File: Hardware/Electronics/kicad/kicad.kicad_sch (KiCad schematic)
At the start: 47 parts, among them J1 Conn_01x03_Socket, J2 Conn_01x03_Socket, J3 Conn_01x03_Socket, J6 USB_C_Receptacle_USB2.0_16P, SW1 SW_Push, SW2 SW_Push, SW3 SW_Push, U1 USBLC6-2P6, U2 MCP73831-2-OT, U3 ESP32-C3-MINI-1-N4, U4 XC6210B332MR, U5 TPS61023DRLR, U6 SN74LV1T34DBV

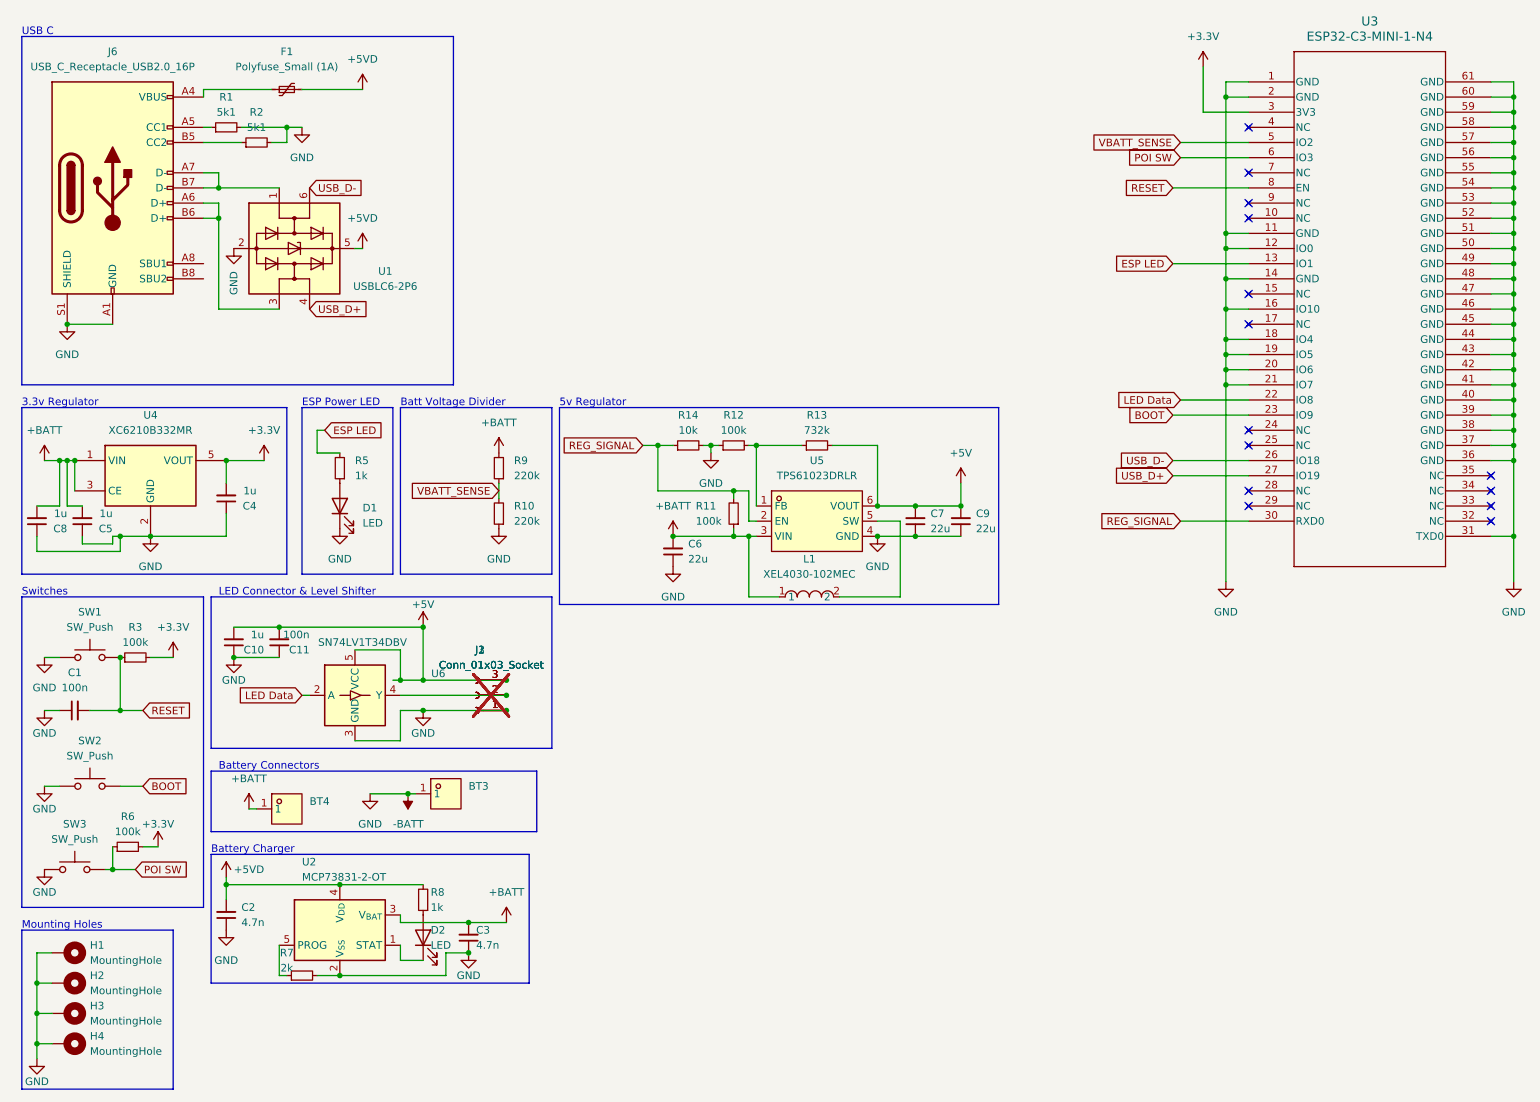
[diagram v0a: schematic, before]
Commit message: Add Clock pinout & FPC connectors to PCB, start on basic ws2812b LED strip.
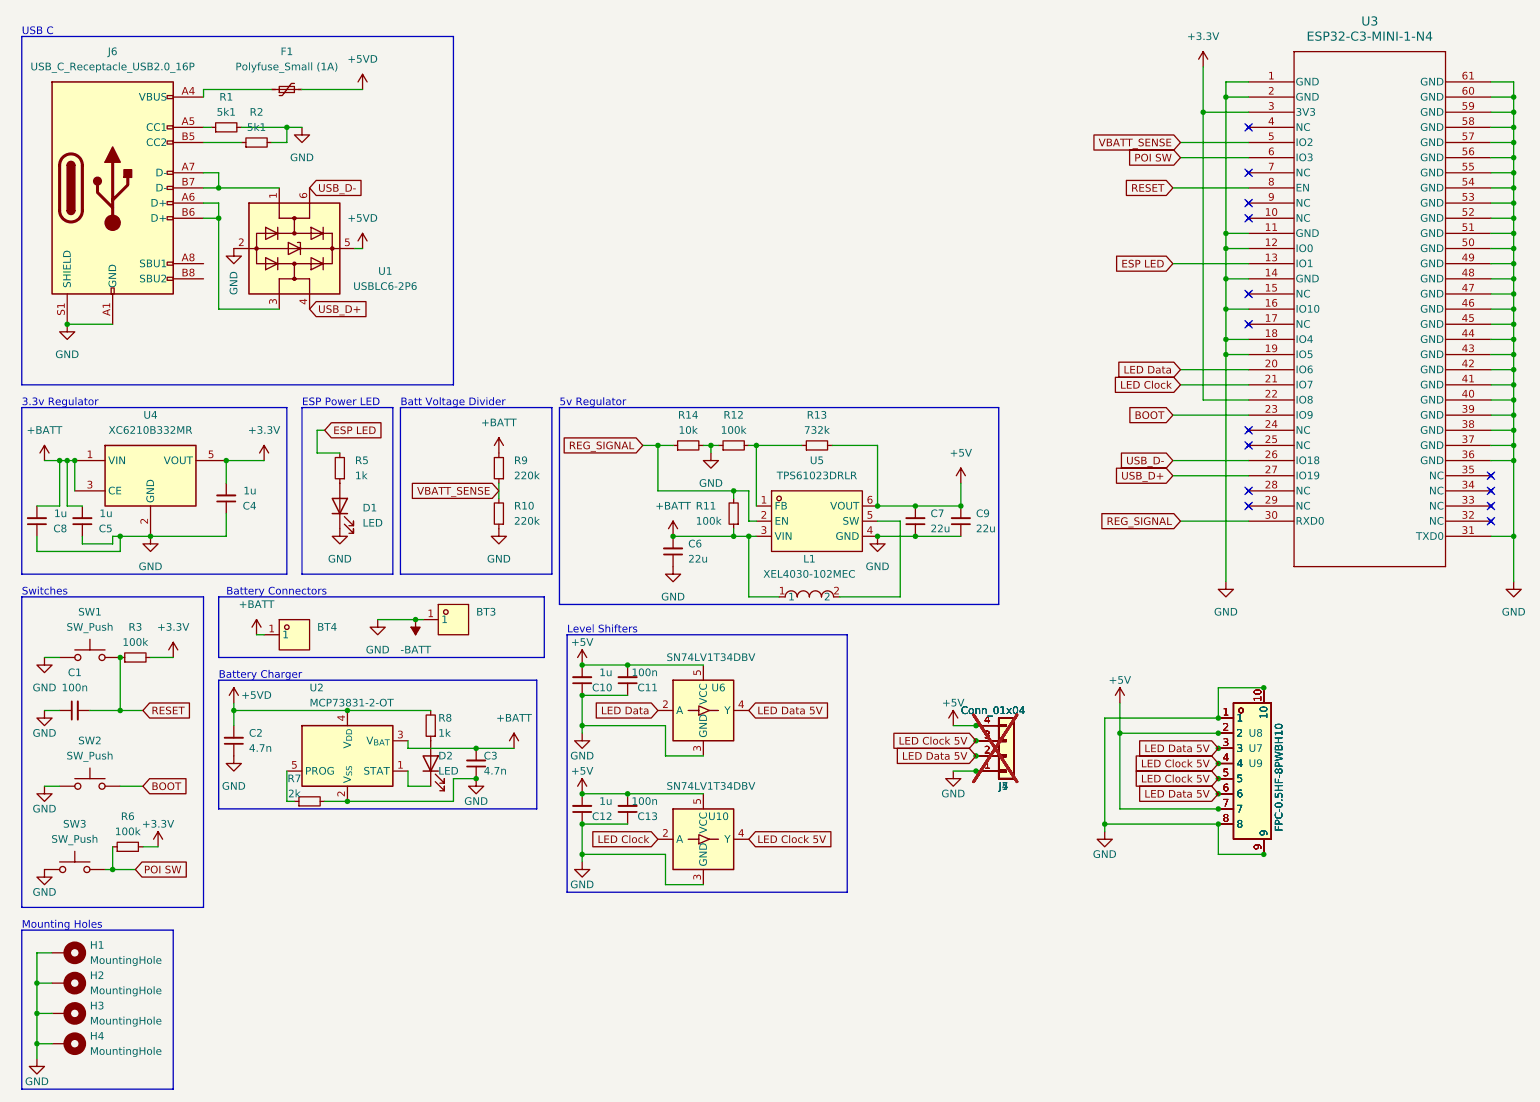
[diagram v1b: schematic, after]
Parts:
- removed J1, J2, J3: Conn_01x03_Socket, Connector_JST:JST_PH_B3B-PH-K_1x03_P2.00mm_Vertical, symbol Connector:Conn_01x03_Socket
- added C12: 1u, Capacitor_SMD:C_0805_2012Metric, symbol Device:C_Small
- added C13: 100n, Capacitor_SMD:C_0805_2012Metric, symbol Device:C_Small
- added J4, J5, J7: Conn_01x04, Connector_PinHeader_2.00mm:PinHeader_1x04_P2.00mm_Vertical, symbol Connector_Generic:Conn_01x04
- added U10: SN74LV1T34DBV, Package_TO_SOT_SMD:SOT-23-5, symbol Logic_LevelTranslator:SN74LV1T34DBV
- added U7, U8, U9: FPC-0.5HF-8PWBH10, easyeda2kicad:FPC-SMD_8P-P0.50_XUNPU_FPC-0.5HF-8PWBH10, symbol easyeda2kicad:FPC-0.5HF-8PWBH10
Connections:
- net +3.3V: now also U3.22 (IO8)
- net +5V: now also C12.2, C13.2, J4.4 (Pin_4), J5.4 (Pin_4), J7.4 (Pin_4), U10.5 (VCC), U7.2, U7.7, U8.2, U8.7, U9.2, U9.7
- net -BATT: now also C12.1, C13.1, J4.1 (Pin_1), J5.1 (Pin_1), J7.1 (Pin_1), U10.3 (GND), U7.1, U7.10, U7.8, U7.9, U8.1, U8.10, U8.8, U8.9, U9.1, U9.10, U9.8, U9.9; no longer U3.20 (IO6), U3.21 (IO7)
- net LED Data: now also U3.20 (IO6); no longer U3.22 (IO8)
- net LED Data 5V: now reaches U6.4 (Y)
- net LED Data 5V: now also J4.2 (Pin_2), J5.2 (Pin_2), J7.2 (Pin_2), U7.3, U7.6, U8.3, U8.6, U9.3, U9.6
- new net LED Clock: U10.2 (A), U3.21 (IO7)
- new net LED Clock 5V: J4.3 (Pin_3), J5.3 (Pin_3), J7.3 (Pin_3), U10.4 (Y), U7.4, U7.5, U8.4, U8.5, U9.4, U9.5
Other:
- note added: "Level Shifters"
- note removed: "LED Connector & Level Shifter"
- moved on the sheet: BT3, BT4, C10, C11, C2, C3, D2, R7, R8, U2, U6

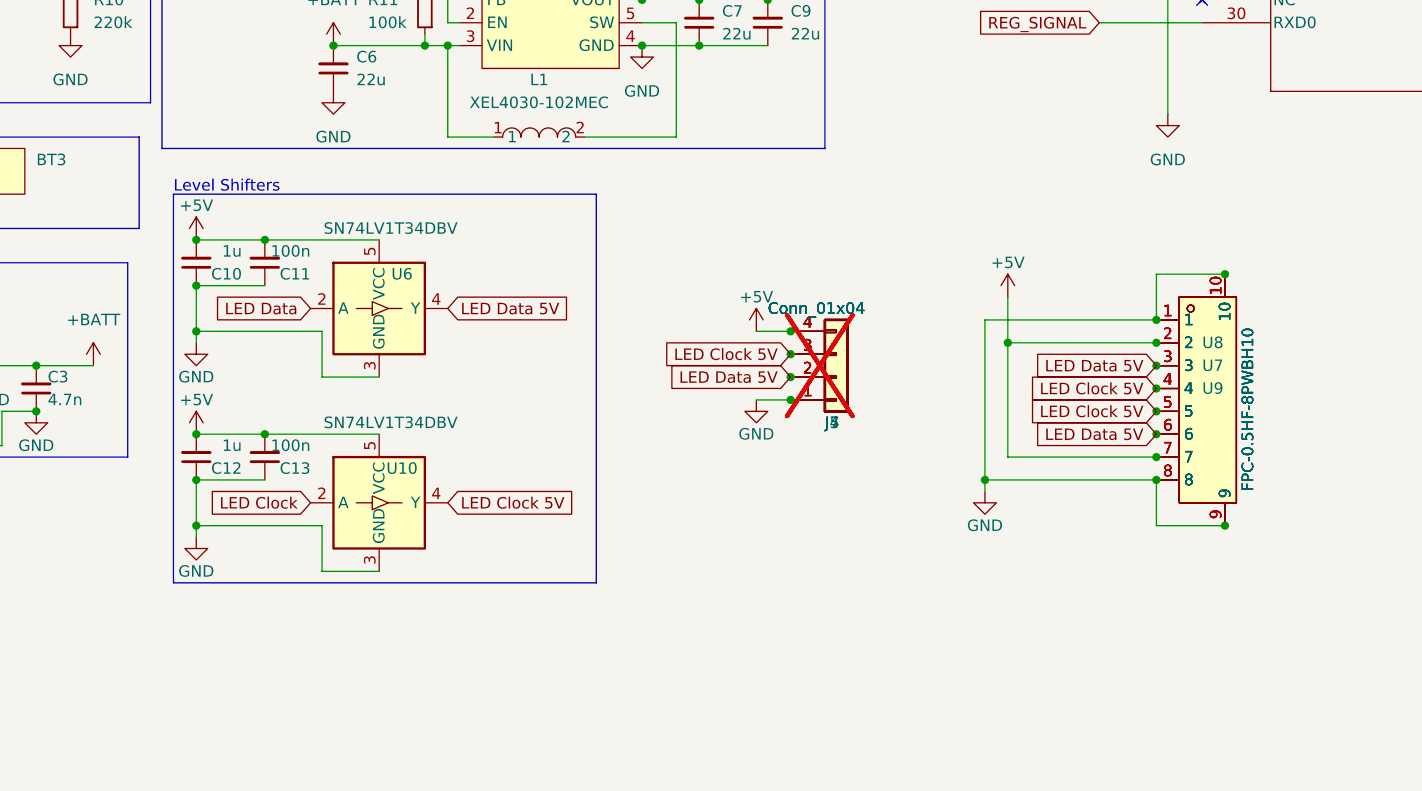
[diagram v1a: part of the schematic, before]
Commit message: Add 20 and 55 pixel strips
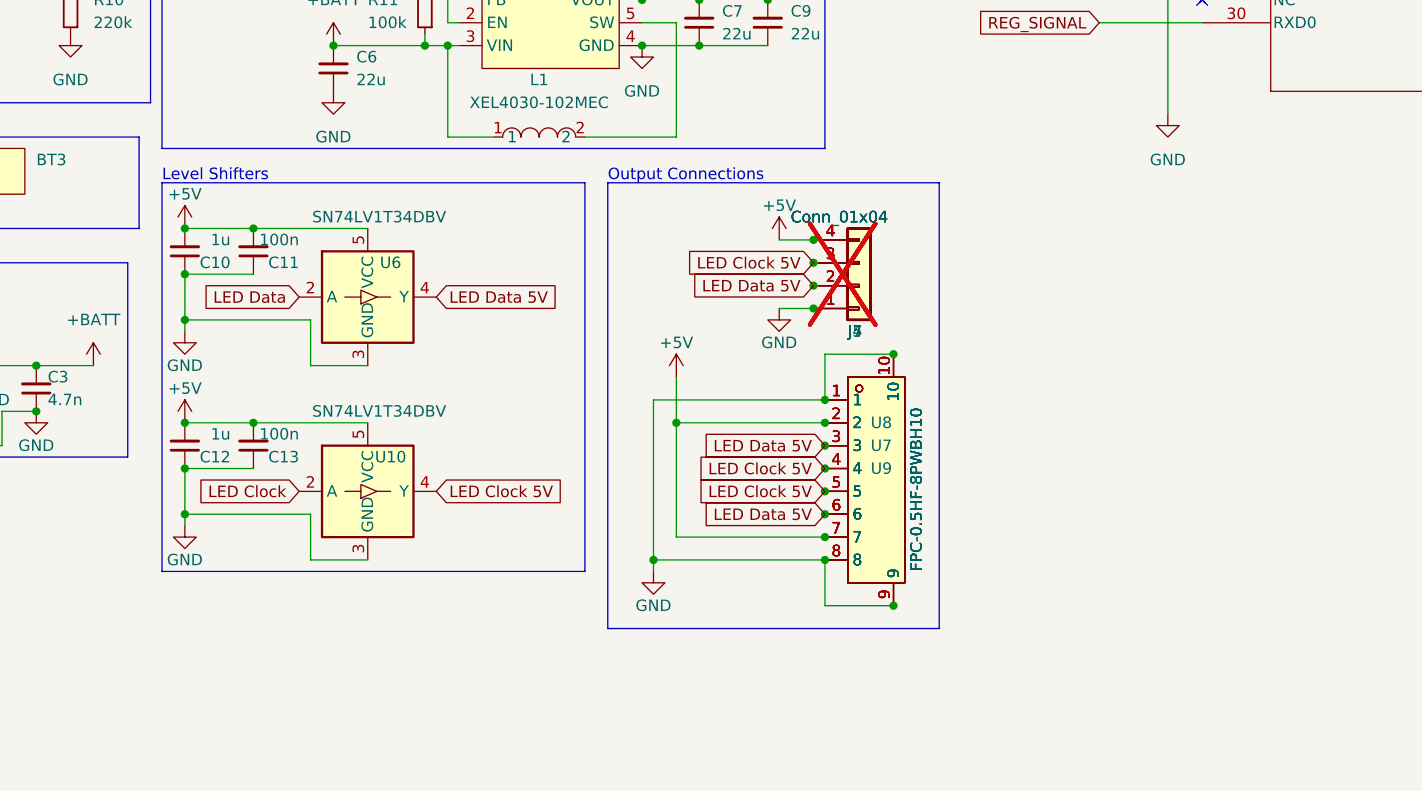
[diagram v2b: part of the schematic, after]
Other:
- note added: "Output Connections"
- moved on the sheet: C10, C11, C12, C13, J4, J5, J7, U10, U6, U7, U8, U9
